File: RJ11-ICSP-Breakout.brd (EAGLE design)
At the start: 23 x 25.4 mm, 2 parts, among them J5 ICSP

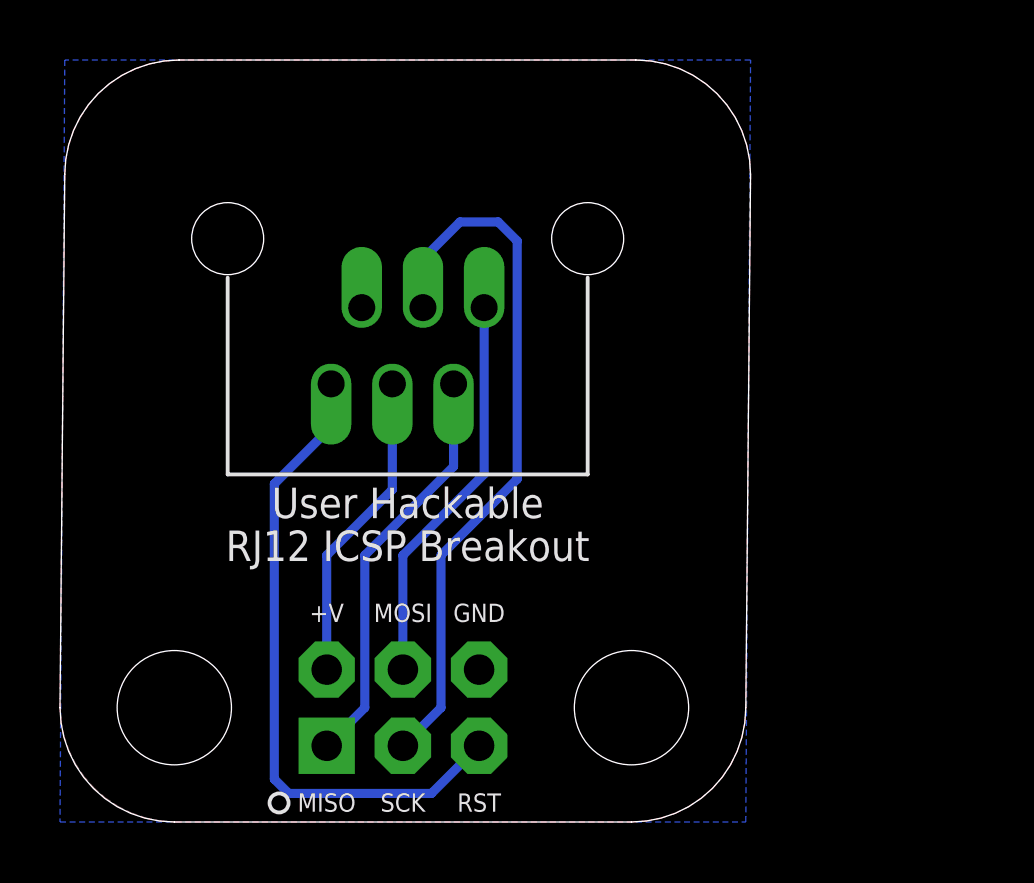
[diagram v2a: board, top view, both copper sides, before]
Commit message: fixing ICSP breakout border
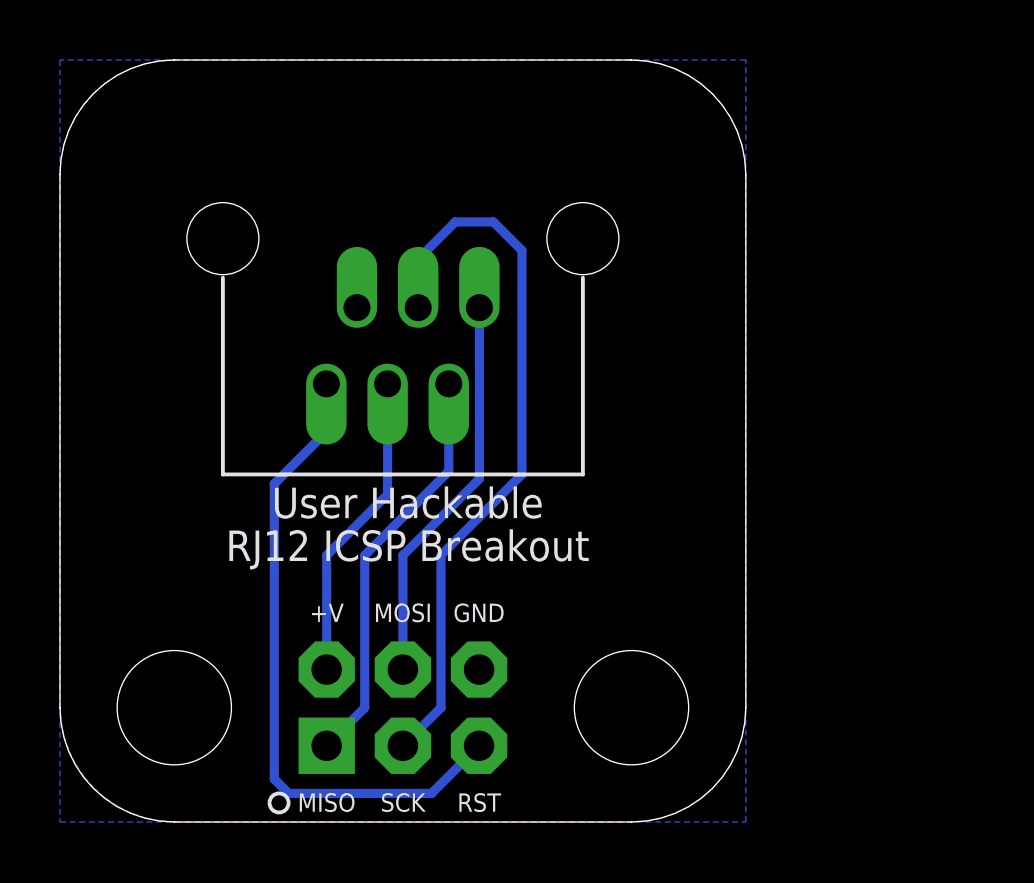
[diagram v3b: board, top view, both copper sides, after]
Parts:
- moved U$7 0.16 mm to (11.4, 17.1)
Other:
- board size 23 x 25.4 mm -> 22.9 x 25.4 mm
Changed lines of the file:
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@@
 <wire x1="3.81" y1="0" x2="19.05" y2="0" width="0" layer="20"/>
 <wire x1="19.05" y1="0" x2="22.86" y2="3.81" width="0" layer="20" curve="90"/>
-<wire x1="22.86" y1="3.81" x2="23.01875" y2="21.57679375" width="0" layer="20"/>
-<wire x1="23.01875" y1="21.57679375" x2="19.19554375" y2="25.4" width="0" layer="20" curve="90"/>
-<wire x1="19.19554375" y1="25.4" x2="3.96875" y2="25.4" width="0" layer="20"/>
-<wire x1="3.96875" y1="25.4" x2="0.15875" y2="21.59" width="0" layer="20" curve="90"/>
-<wire x1="0.15875" y1="21.59" x2="0" y2="3.81" width="0" layer="20"/>
+<wire x1="22.86" y1="3.81" x2="22.86" y2="21.57679375" width="0" layer="20"/>
+<wire x1="22.86" y1="21.57679375" x2="19.03679375" y2="25.4" width="0" layer="20" curve="90"/>
+<wire x1="19.03679375" y1="25.4" x2="3.81" y2="25.4" width="0" layer="20"/>
+<wire x1="3.81" y1="25.4" x2="0" y2="21.59" width="0" layer="20" curve="90"/>
+<wire x1="0" y1="21.59" x2="0" y2="3.81" width="0" layer="20"/>
 <wire x1="0" y1="3.81" x2="3.81" y2="0" width="0" layer="20" curve="90"/>
 <hole x="3.81" y="3.81" drill="3.81"/>
@@
 <elements>
 <element name="J5" library="barbary_enterprises" package="2X3-NS" value="ICSP" x="11.43" y="3.81"/>
-<element name="U$7" library="barbary_enterprises" package="RJ12" value="RJ12" x="11.58875" y="17.145" rot="R180"/>
+<element name="U$7" library="barbary_enterprises" package="RJ12" value="RJ12" x="11.43" y="17.145" rot="R180"/>
 </elements>
 <signals>
@@
 <contactref element="J5" pad="6"/>
 <polygon width="0.4064" layer="1" isolate="0.3048">
-<vertex x="19.19554375" y="25.4"/>
-<vertex x="3.98195625" y="25.4" curve="90"/>
-<vertex x="0.15875" y="21.57679375"/>
+<vertex x="19.03679375" y="25.4"/>
+<vertex x="3.82320625" y="25.4" curve="90"/>
+<vertex x="0" y="21.57679375"/>
 <vertex x="0" y="3.862553125" curve="90"/>
 <vertex x="3.862553125" y="0"/>
 <vertex x="19.05" y="0" curve="90"/>
 <vertex x="22.86" y="3.81"/>
-<vertex x="23.01875" y="21.57679375" curve="90"/>
+<vertex x="22.86" y="21.57679375" curve="90"/>
 </polygon>
 <polygon width="0.3048" layer="16" isolate="0.3048">
 <vertex x="0" y="0"/>
 <vertex x="22.86" y="0"/>
-<vertex x="23.01875" y="25.4"/>
-<vertex x="0.15875" y="25.4"/>
+<vertex x="22.86" y="25.4"/>
+<vertex x="0" y="25.4"/>
 </polygon>
 <contactref element="U$7" pad="2"/>
@@
 <contactref element="U$7" pad="3"/>
 <wire x1="8.89" y1="5.08" x2="8.89" y2="8.89" width="0.3048" layer="16"/>
-<wire x1="8.89" y1="8.89" x2="11.07875" y2="11.07875" width="0.3048" layer="16"/>
-<wire x1="11.07875" y1="11.07875" x2="11.07875" y2="14.605" width="0.3048" layer="16"/>
+<wire x1="8.89" y1="8.89" x2="10.92" y2="10.92" width="0.3048" layer="16"/>
+<wire x1="10.92" y1="10.92" x2="10.92" y2="14.605" width="0.3048" layer="16"/>
 </signal>
 <signal name="4">
@@
 <wire x1="11.43" y1="2.54" x2="12.7" y2="3.81" width="0.3048" layer="16"/>
 <wire x1="12.7" y1="3.81" x2="12.7" y2="8.89" width="0.3048" layer="16"/>
-<wire x1="12.7" y1="8.89" x2="15.24" y2="11.43" width="0.3048" layer="16"/>
-<wire x1="15.24" y1="11.43" x2="15.24" y2="19.3675" width="0.3048" layer="16"/>
-<wire x1="15.24" y1="19.3675" x2="14.605" y2="20.0025" width="0.3048" layer="16"/>
-<wire x1="14.605" y1="20.0025" x2="13.335" y2="20.0025" width="0.3048" layer="16"/>
-<wire x1="13.335" y1="20.0025" x2="12.065" y2="18.7325" width="0.3048" layer="16"/>
-<wire x1="12.065" y1="18.7325" x2="12.065" y2="17.17875" width="0.3048" layer="16"/>
-<wire x1="12.065" y1="17.17875" x2="12.09875" y2="17.145" width="0.3048" layer="16"/>
+<wire x1="12.7" y1="8.89" x2="15.39875" y2="11.58875" width="0.3048" layer="16"/>
+<wire x1="15.39875" y1="11.58875" x2="15.39875" y2="19.05" width="0.3048" layer="16"/>
+<wire x1="15.39875" y1="19.05" x2="14.44625" y2="20.0025" width="0.3048" layer="16"/>
+<wire x1="14.44625" y1="20.0025" x2="13.17625" y2="20.0025" width="0.3048" layer="16"/>
+<wire x1="13.17625" y1="20.0025" x2="11.90625" y2="18.7325" width="0.3048" layer="16"/>
+<wire x1="11.90625" y1="18.7325" x2="11.90625" y2="17.17875" width="0.3048" layer="16"/>
+<wire x1="11.90625" y1="17.17875" x2="11.94" y2="17.145" width="0.3048" layer="16"/>
 </signal>
 <signal name="5">
@@
 <wire x1="8.89" y1="2.54" x2="10.16" y2="3.81" width="0.3048" layer="16"/>
 <wire x1="10.16" y1="3.81" x2="10.16" y2="8.89" width="0.3048" layer="16"/>
-<wire x1="10.16" y1="8.89" x2="13.11875" y2="11.84875" width="0.3048" layer="16"/>
-<wire x1="13.11875" y1="11.84875" x2="13.11875" y2="14.605" width="0.3048" layer="16"/>
+<wire x1="10.16" y1="8.89" x2="12.96" y2="11.69" width="0.3048" layer="16"/>
+<wire x1="12.96" y1="11.69" x2="12.96" y2="14.605" width="0.3048" layer="16"/>
 </signal>
 <signal name="6">
@@
 <contactref element="U$7" pad="6"/>
 <wire x1="11.43" y1="5.08" x2="11.43" y2="8.89" width="0.3048" layer="16"/>
-<wire x1="11.43" y1="8.89" x2="14.13875" y2="11.59875" width="0.3048" layer="16"/>
-<wire x1="14.13875" y1="11.59875" x2="14.13875" y2="17.145" width="0.3048" layer="16"/>
+<wire x1="11.43" y1="8.89" x2="13.98" y2="11.44" width="0.3048" layer="16"/>
+<wire x1="13.98" y1="11.44" x2="13.98" y2="17.145" width="0.3048" layer="16"/>
 </signal>
 <signal name="RST">
@@
 <wire x1="7.62" y1="0.9525" x2="7.14375" y2="1.42875" width="0.3048" layer="16"/>
 <wire x1="7.14375" y1="1.42875" x2="7.14375" y2="11.27125" width="0.3048" layer="16"/>
-<wire x1="7.14375" y1="11.27125" x2="9.04875" y2="13.17625" width="0.3048" layer="16"/>
-<wire x1="9.04875" y1="13.17625" x2="9.04875" y2="14.595" width="0.3048" layer="16"/>
-<wire x1="9.04875" y1="14.595" x2="9.03875" y2="14.605" width="0.3048" layer="16"/>
+<wire x1="7.14375" y1="11.27125" x2="8.89" y2="13.0175" width="0.3048" layer="16"/>
+<wire x1="8.89" y1="13.0175" x2="8.89" y2="14.595" width="0.3048" layer="16"/>
+<wire x1="8.89" y1="14.595" x2="8.88" y2="14.605" width="0.3048" layer="16"/>
 </signal>
 </signals>
